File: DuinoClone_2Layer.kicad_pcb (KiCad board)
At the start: 2 copper layers, 41.4 x 27.7 mm, 17 parts, among them J1 Digital pins, J2 Serial, J3 ICSP, J4 I2C, U1 DS1337S+, U2 24LC1025, U3 24LC1025, U4 ATMEGA328P-AU, Y1 Crystal 32MHz, Y2 Crystal 16MHz

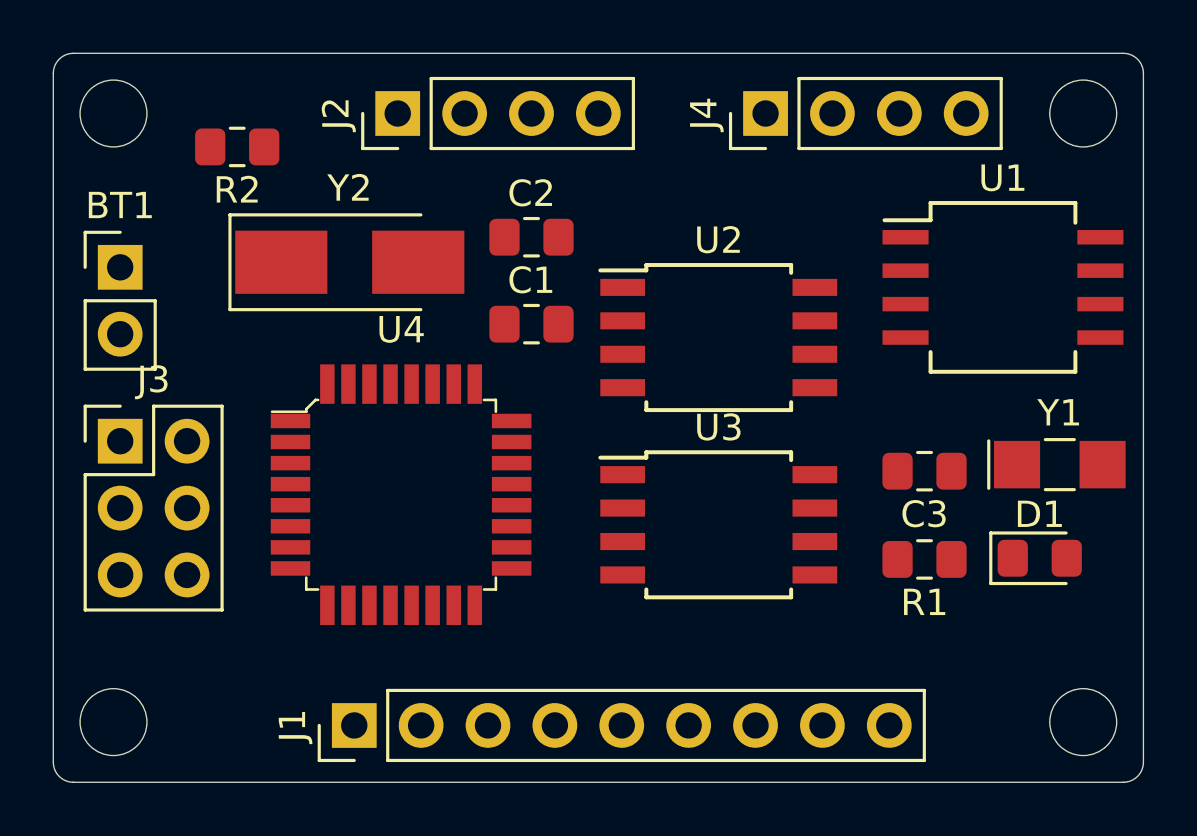
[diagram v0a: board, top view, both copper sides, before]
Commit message: Rerouted board in 2 layers
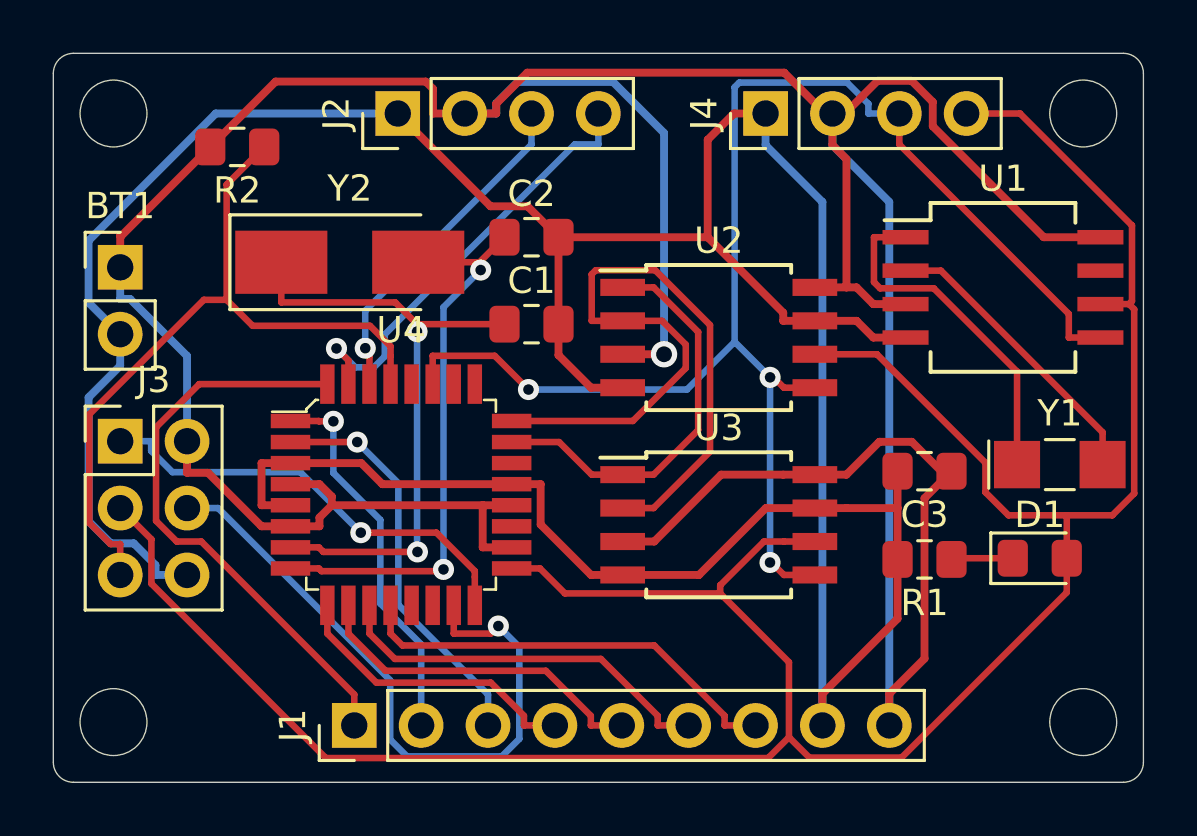
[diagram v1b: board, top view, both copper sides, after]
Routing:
- net /Vcc: track 0.00 -> 153.7 mm, vias 0 -> 1
- net GNDPWR: track 0.00 -> 132.5 mm
- net /SCK: track 0.00 -> 101.6 mm
- net /SDA: track 0.00 -> 55.6 mm, vias 0 -> 3
- net /RESET: track 0.00 -> 28.6 mm
- net /ADDS2: track 0.00 -> 28.5 mm
- net /MOSI: track 0.00 -> 25.6 mm, vias 0 -> 1
- net Net-(C1-Pad1): track 0.00 -> 23.9 mm, vias 0 -> 2
- net /D2: track 0.00 -> 22.2 mm
- net Net-(C2-Pad1): track 0.00 -> 21.9 mm, vias 0 -> 2
- net /MISO: track 0.00 -> 17.0 mm, vias 0 -> 1
- net /TX: track 0.00 -> 17.0 mm, vias 0 -> 1
- net /D8: track 0.00 -> 16.6 mm
- net /ADDS1: track 0.00 -> 15.6 mm
- net /D4: track 0.00 -> 15.4 mm, vias 0 -> 1
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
